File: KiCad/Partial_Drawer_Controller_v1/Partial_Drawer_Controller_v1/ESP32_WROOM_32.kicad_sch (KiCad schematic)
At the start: 37 parts, among them Q1 SS8050, Q2 2N7002T-7-F, Q3 2N7002T-7-F, Q5 SS8050, U6 CP2102N-Axx-xQFN28, U7 ESP32-WROOM-32E_8N, X1 USB-Micro

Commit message: feat: some small progress
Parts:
- removed U7: ESP32-WROOM-32E_8N, Robast_Footprints:XCVR_ESP32-WROOM-32E_(16MB), symbol ESP32-WROOM-32E__16MB_:ESP32-WROOM-32E_(16MB)
- added U7: ESP32-WROOM-32E-N8, Robast:ESP32-WROOM-32E, symbol _MCU:ESP32-WROOM-32E-N8
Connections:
- net +3V3: now also U7.2 (3V3)
- net EN_ESP32: now also U7.3 (EN)
- net GND: now also U7.1 (GND), U7.15 (GND), U7.38 (GND), U7.39_1 (GND), U7.39_2 (GND), U7.39_3 (GND), U7.39_4 (GND), U7.39_5 (GND), U7.39_6 (GND), U7.39_7 (GND), U7.39_8 (GND), U7.39_9 (GND)
- net I34: now also U7.6 (IO34)
- net I35: now also U7.7 (IO35)
- net I36: now also U7.4 (SENSOR_VP)
- net IO0: now also U7.25 (IO0)
- net IO16_UART2_RX: now also U7.27 (IO16)
- net IO17_UART2_TX: now also U7.28 (IO17)
- net IO18_SPI_SCK: now also U7.30 (IO18)
- net IO19_SPI_SO: now also U7.31 (IO19)
- net IO2: now also U7.24 (IO2)
- net IO21_SDA: now also U7.33 (IO21)
- net IO22_SCL: now also U7.36 (IO22)
- net IO23_SPI_SI: now also U7.37 (IO23)
- net IO25_DAC_1: now also U7.10 (IO25)
- net IO26_DAC_2: now also U7.11 (IO26)
- net IO27: now also U7.12 (IO27)
- net IO32: now also U7.8 (IO32)
- net IO33: now also U7.9 (IO33)
- net IO4: now also U7.26 (IO4)
- net IO5_SPI_CS: now also U7.29 (IO5)
- net RXD0: now also U7.34 (RXD0)
- net TXD0: now also U7.35 (TXD0)
- net pe_2_~INT: now also U7.5 (SENSOR_VN)
- new net: U7.17 (NC), U7.18 (NC), U7.19 (NC), U7.20 (NC), U7.21 (NC), U7.22 (NC)
- new net IO12_TDI: U7.14 (IO12)
- new net IO13_TCK: U7.16 (IO13)
- new net IO14_TMS: U7.13 (IO14)
- new net IO15_TDO: U7.23 (IO15)
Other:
- note added: "FT2232H Debugging ESP32"
- note added: "JTAG Debug Interface"
- note added: "More information:"

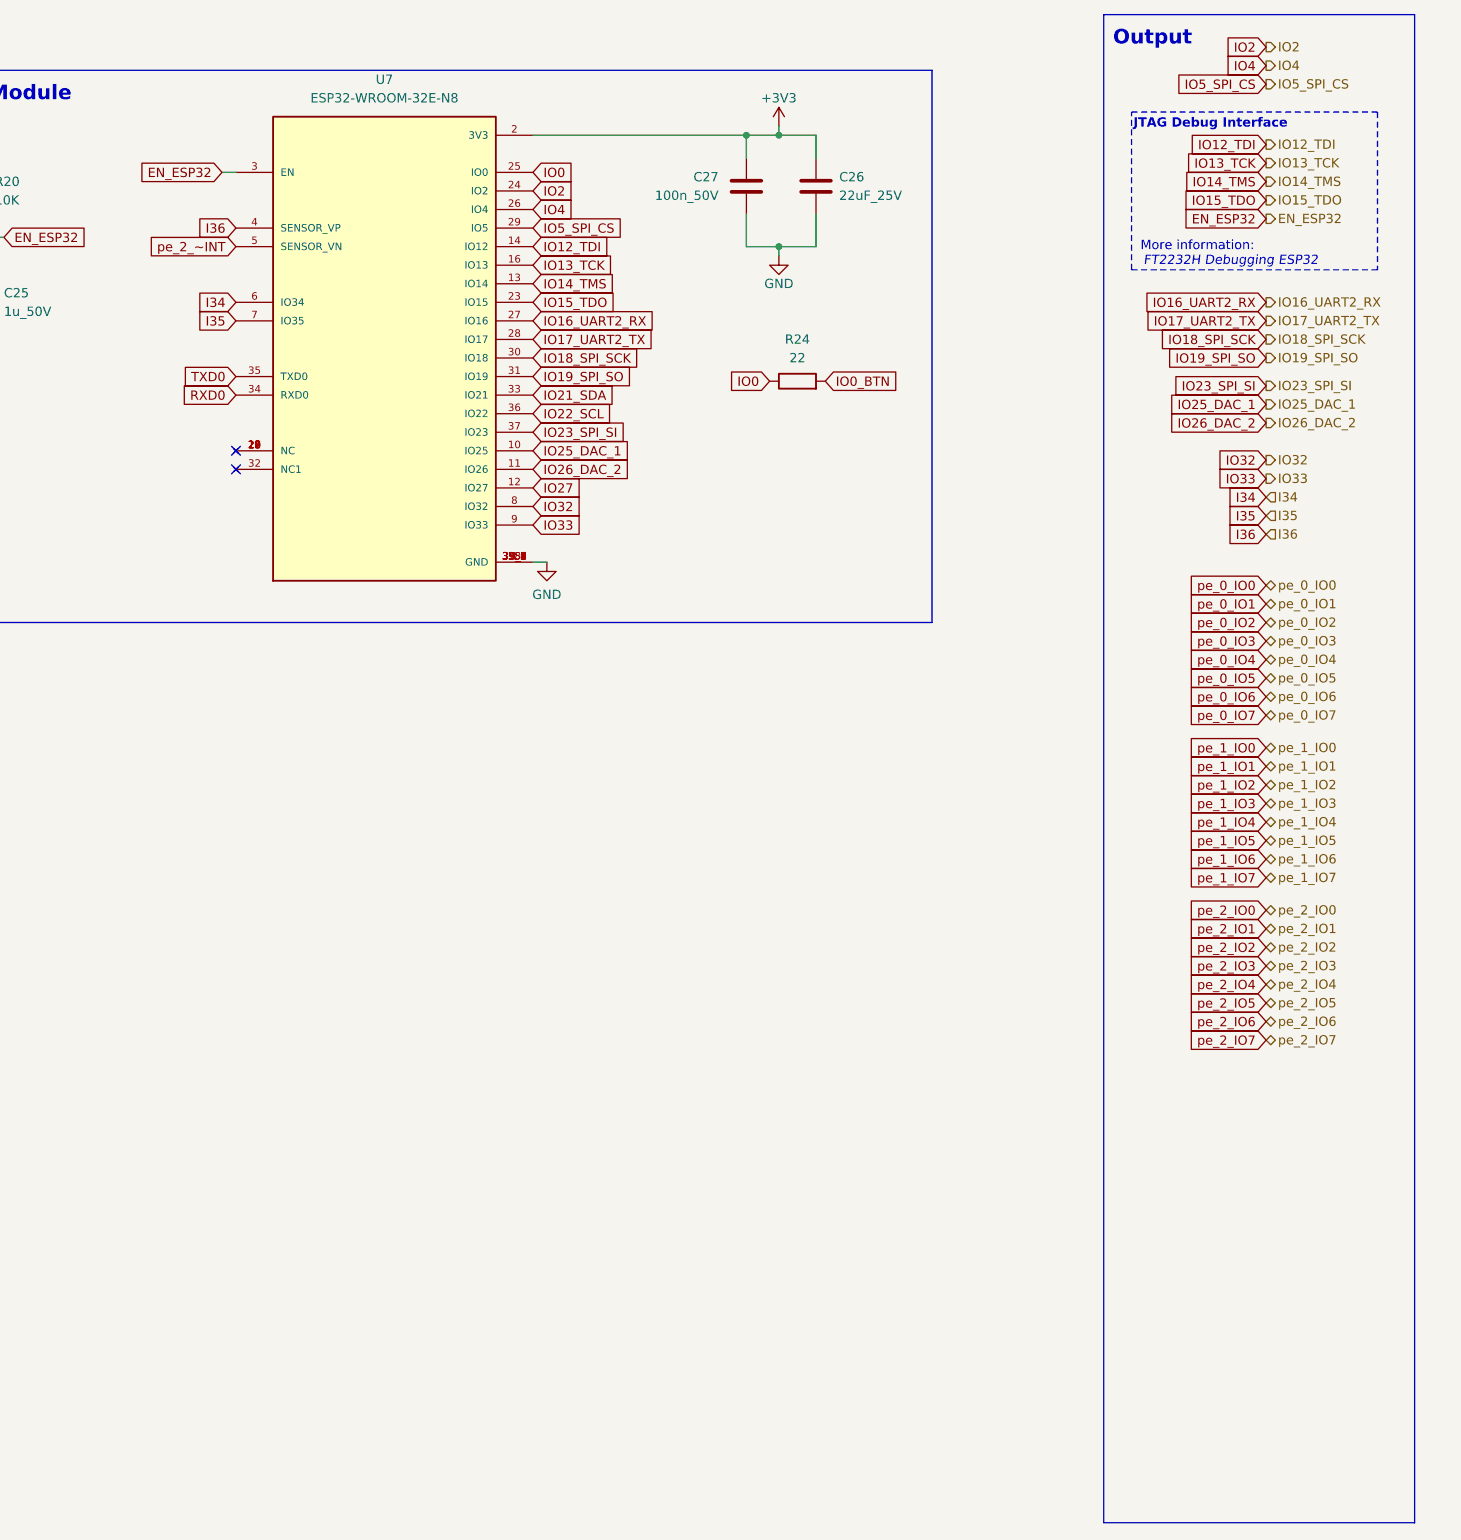
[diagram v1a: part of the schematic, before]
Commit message: feat: started to replace CAN Communication chip to `SN65HVD230` and added todos
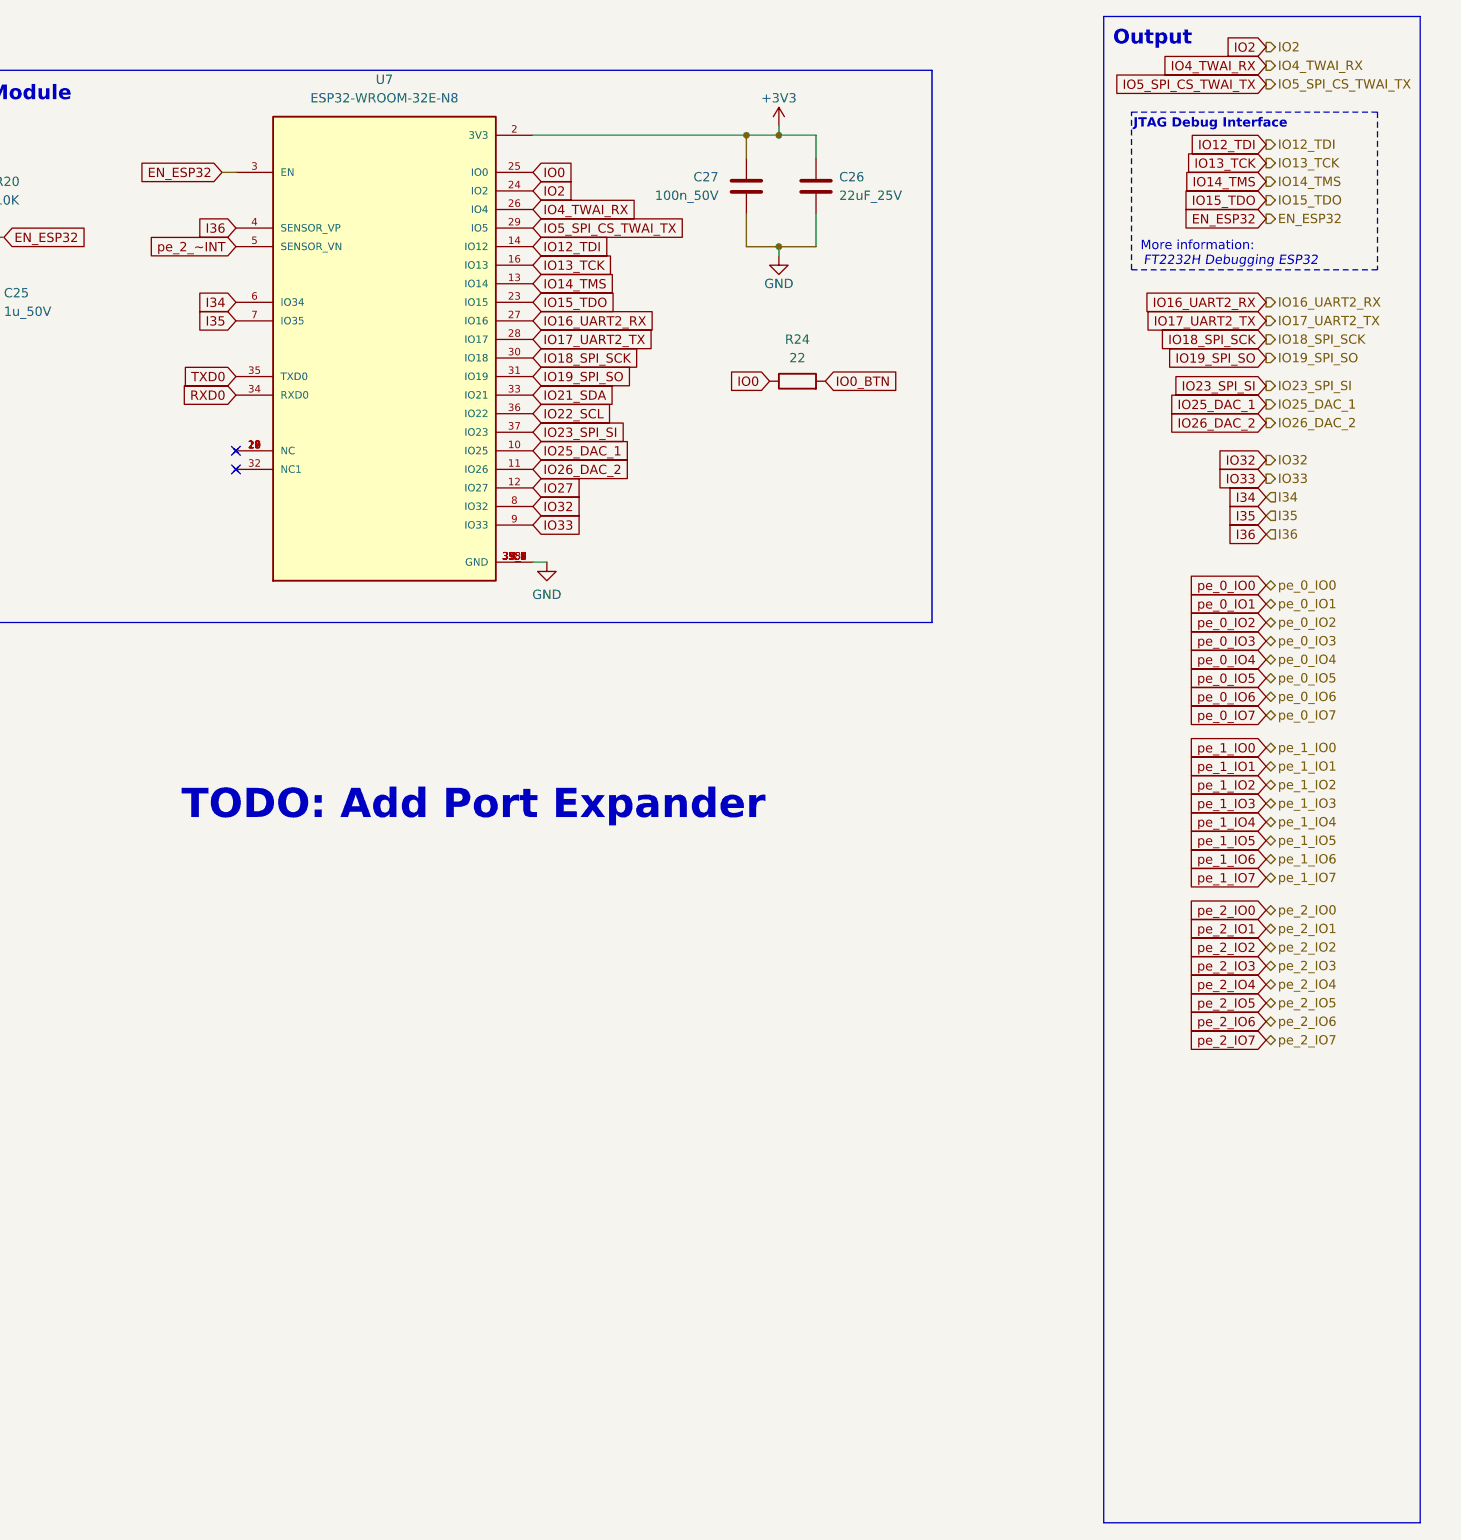
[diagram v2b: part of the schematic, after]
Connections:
- net IO4 renamed IO4_TWAI_RX
- net IO5_SPI_CS renamed IO5_SPI_CS_TWAI_TX
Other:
- note added: "TODO: Add Port Expander"
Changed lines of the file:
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@@
 	)
 	(rectangle
-		(start 362.585 13.97)
-		(end 405.13 220.345)
+		(start 362.585 14.224)
+		(end 405.892 220.345)
 		(stroke
 			(width 0)
@@
 		)
 	)
+	(text "TODO: Add Port Expander"
+		(exclude_from_sim no)
+		(at 276.352 122.174 0)
+		(effects
+			(font
+				(size 4 4)
+				(bold yes)
+				(color 255 0 0 1)
+			)
+		)
+	)
 	(text "Input"
 		(exclude_from_sim no)
@@
 		)
 	)
-	(global_label "IO5_SPI_CS"
+	(global_label "IO5_SPI_CS_TWAI_TX"
 		(shape input)
 		(at 384.81 23.495 180)
@@
 		)
 		(property "Intersheetrefs" "${INTERSHEET_REFS}"
-			(at 371.2604 23.495 0)
+			(at 362.9563 23.495 0)
 			(effects
 				(font
@@
 		)
 	)
-	(global_label "IO5_SPI_CS"
+	(global_label "IO5_SPI_CS_TWAI_TX"
 		(shape input)
 		(at 284.48 43.18 0)
@@
 		)
 		(property "Intersheetrefs" "${INTERSHEET_REFS}"
-			(at 298.0296 43.18 0)
+			(at 306.3337 43.18 0)
 			(effects
 				(font
@@
 		)
 	)
-	(global_label "IO4"
+	(global_label "IO4_TWAI_RX"
 		(shape input)
 		(at 384.81 20.955 180)
@@
 		)
 		(property "Intersheetrefs" "${INTERSHEET_REFS}"
-			(at 378.7594 20.955 0)
+			(at 370.1529 20.955 0)
 			(effects
 				(font
@@
 		)
 	)
-	(global_label "IO4"
+	(global_label "IO4_TWAI_RX"
 		(shape input)
 		(at 284.48 40.64 0)
@@
 		)
 		(property "Intersheetrefs" "${INTERSHEET_REFS}"
-			(at 290.5306 40.64 0)
+			(at 299.1371 40.64 0)
 			(effects
 				(font
@@
 		)
 	)
-	(hierarchical_label "IO4"
+	(hierarchical_label "IO4_TWAI_RX"
 		(shape output)
 		(at 384.81 20.955 0)
@@
 		)
 	)
-	(hierarchical_label "IO5_SPI_CS"
+	(hierarchical_label "IO5_SPI_CS_TWAI_TX"
 		(shape output)
 		(at 384.81 23.495 0)

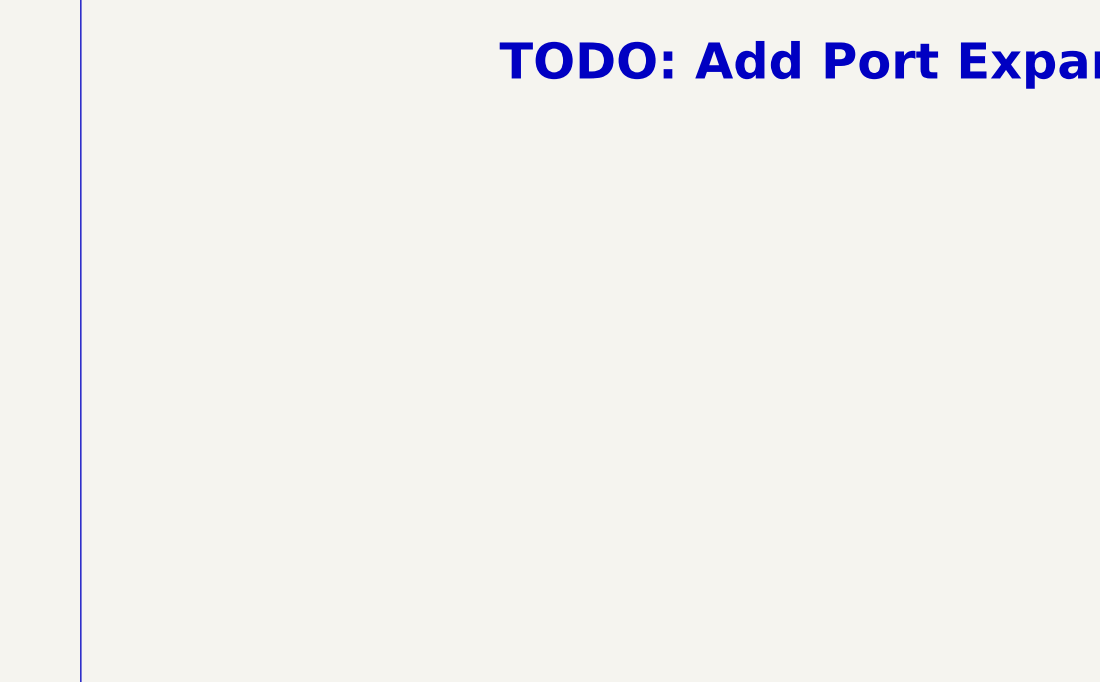
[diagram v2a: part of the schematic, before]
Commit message: feat: starting to add port expander (WIP)
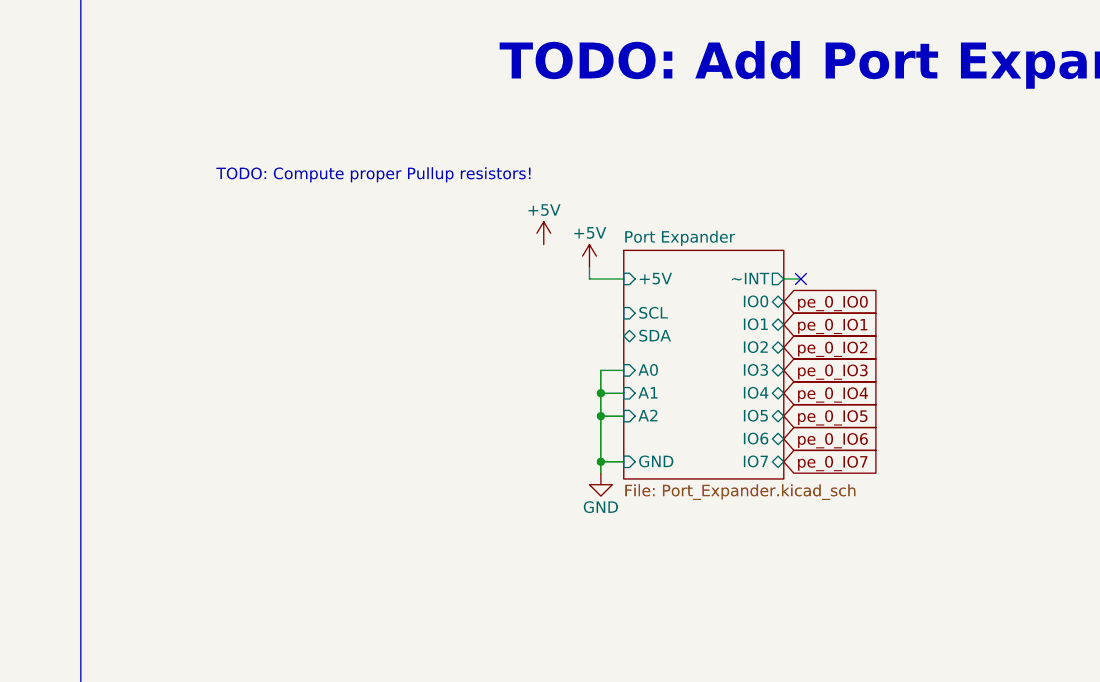
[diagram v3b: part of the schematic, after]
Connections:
- no-connect marks 18 -> 19
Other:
- added sheet Port Expander (Port_Expander.kicad_sch)
- note added: "TODO: Compute proper Pullup resistors!"
